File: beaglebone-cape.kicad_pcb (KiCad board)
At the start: 2 copper layers, 86.4 x 54.6 mm, 56 parts, among them P1 BEAGLEBONE_BLACK, P4 JUMPERS, P6 CONN_01X05, Q1 2N7000, Q2 2N7000, Q3 2N7000, Q4 2N7000, SW1 PWR_SWITCH, SW2 RESET_SWITCH, U1 24C256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

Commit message: Changed all power track widths to 2mm, made slight path change to 5V net
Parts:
- renumbered SW1 to POWER, SW2 to RESET
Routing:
- net +5V: track 88.3 -> 77.5 mm
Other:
- net class 5V Power: trace_width 1.5 -> 2
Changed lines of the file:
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@@
   (net_class "5V Power" ""
     (clearance 0.2286)
-    (trace_width 1.5)
+    (trace_width 2)
     (via_dia 0.889)
     (via_drill 0.635)
@@
   (module hocuspocus:BUTTON_MJTP1230 (layer F.Cu)
     (at 108.5 90.25 270)
-    (fp_text reference SW1 (at 0.25 -4 270) (layer F.SilkS)
+    (fp_text reference POWER (at -0.08 3.725 270) (layer F.SilkS)
       (effects (font (size 1 1) (thickness 0.15)))
     )
@@
   (module hocuspocus:BUTTON_MJTP1230 (layer F.Cu)
     (at 99.5 90.25 270)
-    (fp_text reference SW2 (at 0.25 -4 270) (layer F.SilkS)
+    (fp_text reference RESET (at -0.08 3.615 270) (layer F.SilkS)
       (effects (font (size 1 1) (thickness 0.15)))
     )
@@
   (segment (start 158.837 130.81) (end 162.56 130.81) (width 2) (layer B.Cu) (net 9))
   (segment (start 149.86 130.81) (end 158.837 130.81) (width 2) (layer B.Cu) (net 9) (status 10))
-  (segment (start 144.78 112.51) (end 144.78 122.555) (width 1.5) (layer B.Cu) (net 10))
-  (segment (start 144.78 122.555) (end 144.78 124.46) (width 1.5) (layer B.Cu) (net 10))
-  (segment (start 130.81 110.49) (end 133.11767 110.49) (width 1.5) (layer B.Cu) (net 10))
-  (segment (start 133.11767 110.49) (end 144.78 122.15233) (width 1.5) (layer B.Cu) (net 10))
-  (segment (start 144.78 122.15233) (end 144.78 122.555) (width 1.5) (layer B.Cu) (net 10))
-  (segment (start 130.81 110.49) (end 130.81 107.44708) (width 1.5) (layer B.Cu) (net 10))
-  (segment (start 144.78 124.46) (end 144.78 130.81) (width 1.5) (layer B.Cu) (net 10))
-  (segment (start 138.176 119.75) (end 140.07 119.75) (width 1.5) (layer B.Cu) (net 10))
-  (segment (start 140.07 119.75) (end 144.78 124.46) (width 1.5) (layer B.Cu) (net 10))
-  (segment (start 138.195 105.925) (end 144.78 112.51) (width 1.5) (layer B.Cu) (net 10))
-  (segment (start 119.253 135.255) (end 119.253 137.795) (width 1.5) (layer B.Cu) (net 10))
-  (segment (start 119.253 135.255) (end 123.698 130.81) (width 1.5) (layer B.Cu) (net 10))
-  (segment (start 123.698 130.81) (end 130.175 130.81) (width 1.5) (layer B.Cu) (net 10))
-  (segment (start 135.255 130.81) (end 130.175 130.81) (width 1.5) (layer B.Cu) (net 10))
-  (segment (start 135.255 130.81) (end 144.78 130.81) (width 1.5) (layer B.Cu) (net 10))
+  (segment (start 138.195 105.925) (end 132.33208 105.925) (width 2) (layer B.Cu) (net 10))
+  (segment (start 132.33208 105.925) (end 130.81 107.44708) (width 2) (layer B.Cu) (net 10))
+  (segment (start 144.78 112.51) (end 144.78 122.555) (width 2) (layer B.Cu) (net 10))
+  (segment (start 144.78 122.555) (end 144.78 124.46) (width 2) (layer B.Cu) (net 10))
+  (segment (start 144.78 122.15233) (end 144.78 122.555) (width 2) (layer B.Cu) (net 10))
+  (segment (start 130.81 110.49) (end 130.81 107.44708) (width 2) (layer B.Cu) (net 10))
+  (segment (start 144.78 124.46) (end 144.78 130.81) (width 2) (layer B.Cu) (net 10))
+  (segment (start 138.176 119.75) (end 140.07 119.75) (width 2) (layer B.Cu) (net 10))
+  (segment (start 140.07 119.75) (end 144.78 124.46) (width 2) (layer B.Cu) (net 10))
+  (segment (start 138.195 105.925) (end 144.78 112.51) (width 2) (layer B.Cu) (net 10))
+  (segment (start 119.253 135.255) (end 119.253 137.795) (width 2) (layer B.Cu) (net 10))
+  (segment (start 119.253 135.255) (end 123.698 130.81) (width 2) (layer B.Cu) (net 10))
+  (segment (start 123.698 130.81) (end 130.175 130.81) (width 2) (layer B.Cu) (net 10))
+  (segment (start 135.255 130.81) (end 130.175 130.81) (width 2) (layer B.Cu) (net 10))
+  (segment (start 135.255 130.81) (end 144.78 130.81) (width 2) (layer B.Cu) (net 10))
   (segment (start 165.735 128.27) (end 165.735 127.282172) (width 0.254) (layer B.Cu) (net 11))
   (segment (start 165.735 127.282172) (end 165.182827 126.729999) (width 0.254) (layer B.Cu) (net 11))

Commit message: layin pipe
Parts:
- moved R19 27.1 mm to (120.4, 93.2), turned to 90 degrees
- moved R18 20.9 mm to (141.2, 92.7), turned to 90 degrees
- moved P4 16.8 mm to (115.8, 131.6)
- moved R16 16.3 mm to (144.3, 92.7)
- moved R1 16.2 mm to (103.4, 122.4), turned to 270 degrees
- moved R17 11.0 mm to (117.3, 93.2), turned to 90 degrees
- moved R3 10.1 mm to (100.3, 122.4), turned to 270 degrees
- moved R23 9.95 mm to (114.3, 93.2), turned to 90 degrees
- moved R5 7.26 mm to (109.5, 122.4), turned to 270 degrees
- moved R4 7.14 mm to (106.4, 122.4), turned to 270 degrees
- moved U1 6.88 mm to (101.6, 134.1), turned to 90 degrees
- moved R22 6.68 mm to (123.4, 93.2), turned to 90 degrees
- moved R2 6.27 mm to (112.5, 122.4), turned to 270 degrees
- moved C1 4.84 mm to (97.5, 128.5), turned to 270 degrees
- moved R14 3.30 mm to (130.0, 129.5)
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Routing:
- net +3V3: track 0.00 -> 47.8 mm
- net Net-(R21-Pad2): track 30.9 -> 0.00 mm
- net Net-(D5-Pad2): track 0.00 -> 29.8 mm
- net /GPIO_69: track 27.9 -> 0.00 mm
- net /A1: track 0.00 -> 22.8 mm
- net Net-(D6-Pad1): track 0.00 -> 21.3 mm
- net /A2: track 0.00 -> 14.4 mm
- net /A0: track 0.00 -> 10.9 mm
- net Net-(Q2-Pad2): track 4.71 -> 15.1 mm
- net Net-(D5-Pad1): track 0.00 -> 9.66 mm
- net Net-(R20-Pad2): track 39.6 -> 43.3 mm
- net Net-(Q3-Pad2): track 0.00 -> 3.05 mm
- net Net-(D2-Pad2): track 9.31 -> 6.39 mm
- net /I2C2_SDA: track 0.00 -> 2.90 mm
- net /I2C2_SCL: track 0.00 -> 2.90 mm
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
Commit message: Still working on tracks
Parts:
- moved R17 20.7 mm to (138.0, 92.7)
- moved R19 20.7 mm to (141.1, 92.7)
- moved R16 9.27 mm to (135.0, 92.7)
- moved R23 4.47 mm to (118.7, 92.7)
- moved D6 3.21 mm to (121.2, 117.6), turned to 0 degrees
- moved D5 3.14 mm to (121.4, 100.6), turned to 0 degrees
- moved R18 2.92 mm to (144.1, 92.7)
- moved R22 1.73 mm to (121.8, 92.7)
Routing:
- net +3V3: track 47.8 -> 87.7 mm
- net Net-(Q4-Pad2): track 0.00 -> 37.7 mm
- net Net-(R21-Pad2): track 0.00 -> 33.9 mm
- net Net-(D5-Pad1): track 9.66 -> 37.7 mm
- net /GPIO_69: track 0.00 -> 27.8 mm
- net Net-(RLY1-Pad6): track 0.00 -> 24.6 mm
- net /LOCK_RELAYS/R1_READ: track 0.00 -> 23.3 mm
- net /LOCK_RELAYS/R2_READ: track 0.00 -> 20.4 mm
- net (no net): track 0.00 -> 17.8 mm
- net Net-(D6-Pad1): track 21.3 -> 37.5 mm
- net Net-(Q3-Pad2): track 3.05 -> 16.0 mm
- net Net-(P7-Pad1): track 17.4 -> 26.4 mm
- net /SYS_RESETn: track 0.00 -> 6.50 mm
- net /PWR_BUT: track 0.00 -> 6.50 mm
- net /LOCK_RELAYS/R2_ENGAGE: track 0.00 -> 4.35 mm
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
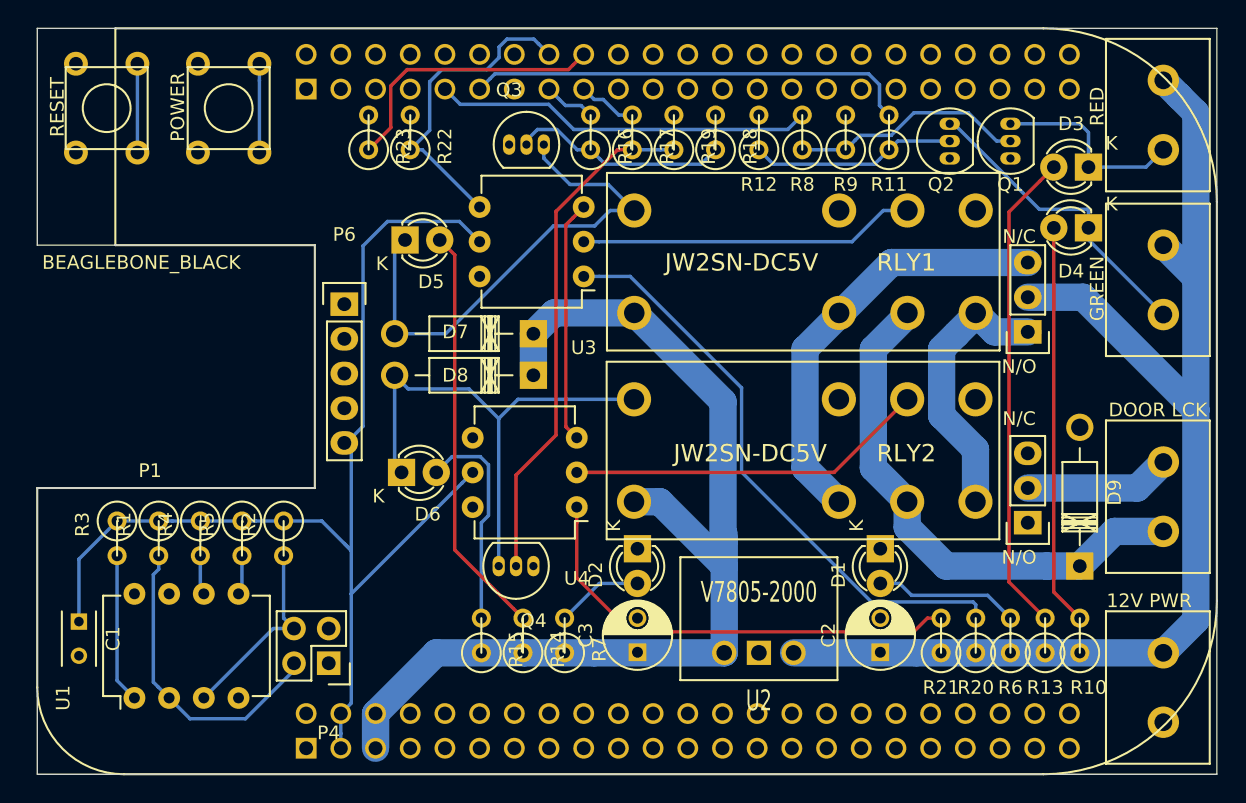
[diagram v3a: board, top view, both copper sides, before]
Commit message: Got DRC check to pass on pcb
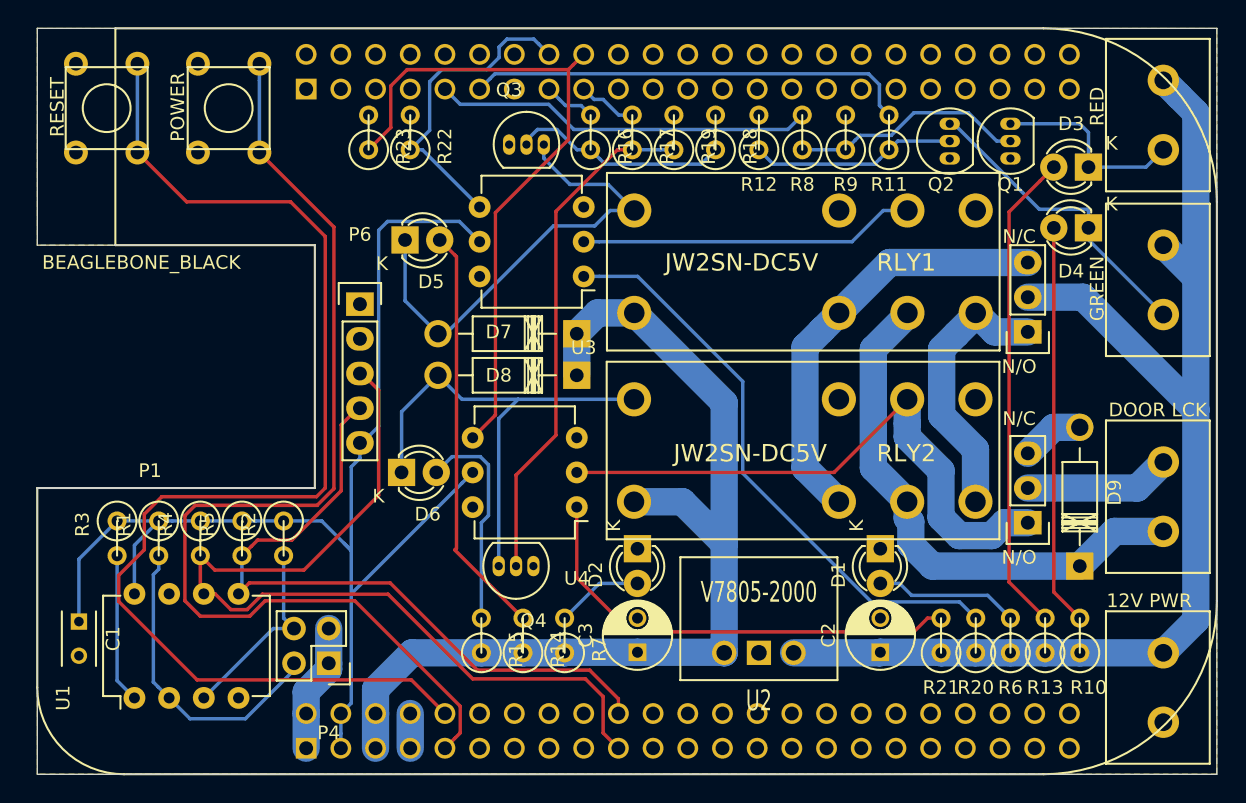
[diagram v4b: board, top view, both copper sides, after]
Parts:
- moved D8 3.18 mm to (134.0, 110.5)
- moved D7 3.18 mm to (134.0, 107.4)
- moved P6 1.14 mm to (118.1, 105.3)
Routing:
- net /SYS_RESETn: track 6.50 -> 89.7 mm
- net /PWR_BUT: track 6.50 -> 79.2 mm
- net /I2C2_SCL: track 2.90 -> 65.8 mm
- net /I2C2_SDA: track 2.90 -> 51.7 mm
- net /LOCK_RELAYS/R2_READ: track 20.4 -> 50.3 mm
- net (no net): track 17.8 -> 0.00 mm
- net Net-(P7-Pad1): track 26.4 -> 43.4 mm
- net GND: track 0.00 -> 14.0 mm
- net +3V3: track 87.7 -> 93.4 mm
- net +5V: track 77.5 -> 74.4 mm
- net /SYS_5V: track 0.00 -> 2.54 mm
- net Net-(D5-Pad1): track 37.7 -> 35.7 mm
- net Net-(D6-Pad1): track 37.5 -> 36.8 mm
- net Net-(D9-Pad1): track 38.3 -> 38.9 mm
- added copper zone on F.Cu, net GND

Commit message: Cleaned up silk screening, adjust module alignment
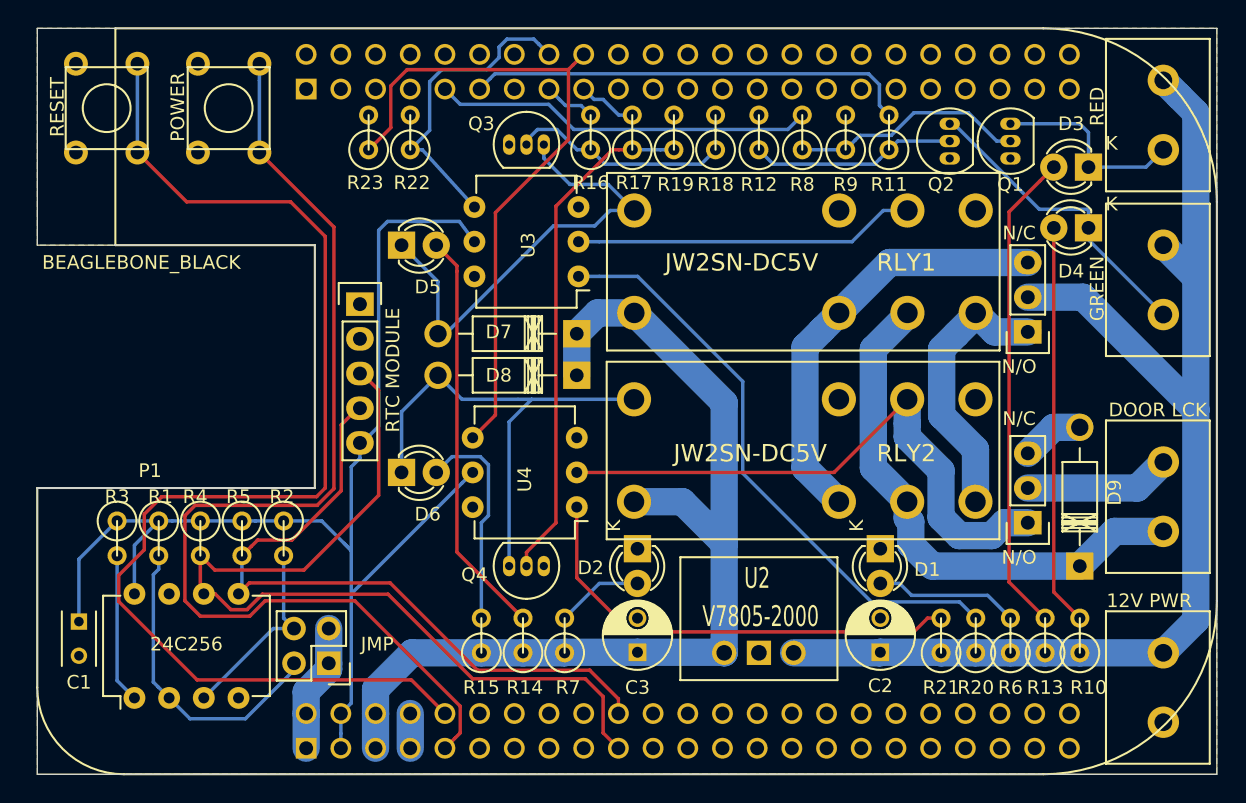
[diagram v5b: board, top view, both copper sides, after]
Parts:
- RTC MODULE: renamed from P6
- moved Q4 0.76 mm to (131.6, 124.5)
- moved D5 0.46 mm to (121.2, 101.0)
- moved U3 0.38 mm to (134.1, 103.3)
- renumbered U1 to 24C256, P4 to JMP
